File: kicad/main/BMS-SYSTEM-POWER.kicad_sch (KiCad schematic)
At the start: 67 parts, among them Q11 2N3904, Q15 IRLML6344TRPBF, Q16 IRLML6344TRPBF, Q17 AO4407A, Q2 AO4407A, Q3 PNP-SOT23, U21 AP64501SP-13, U22 AP64501SP-13, U5 SY8089A

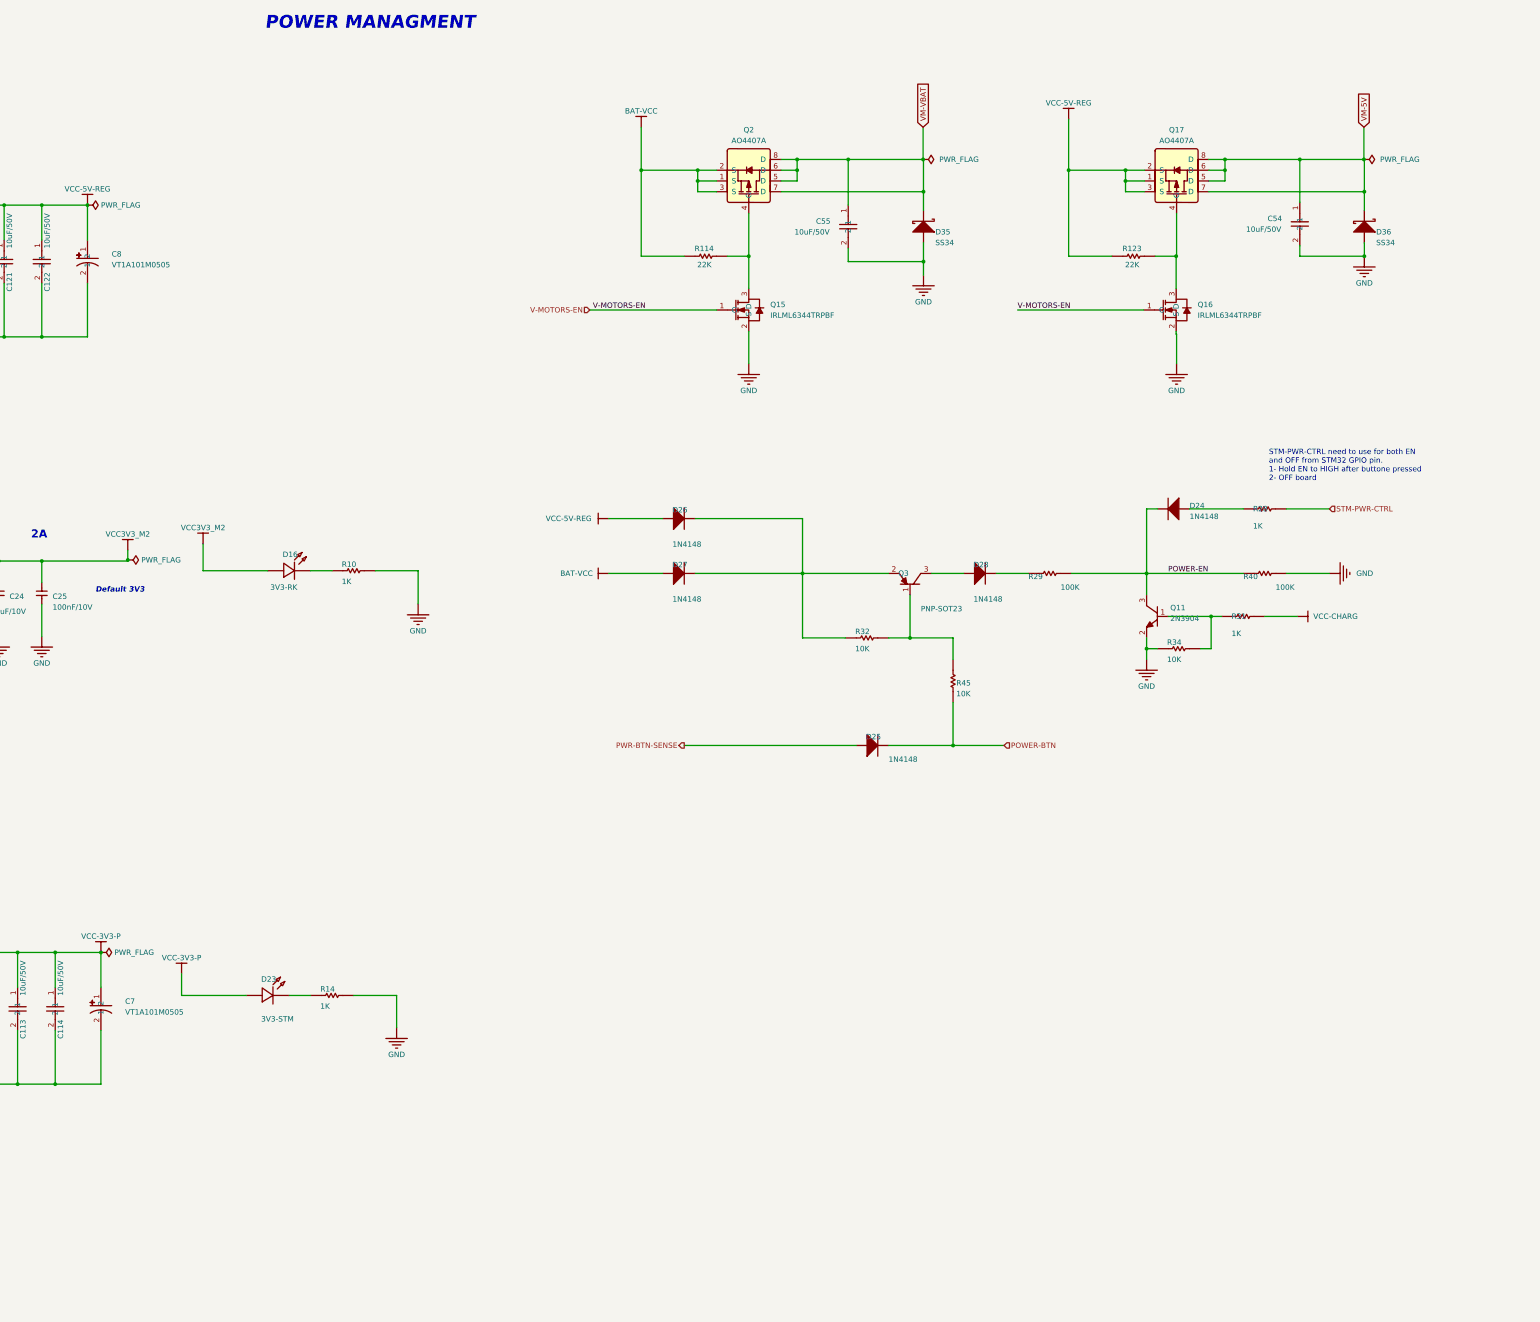
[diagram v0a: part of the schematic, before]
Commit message: Fix edge cut; no-CM STEP
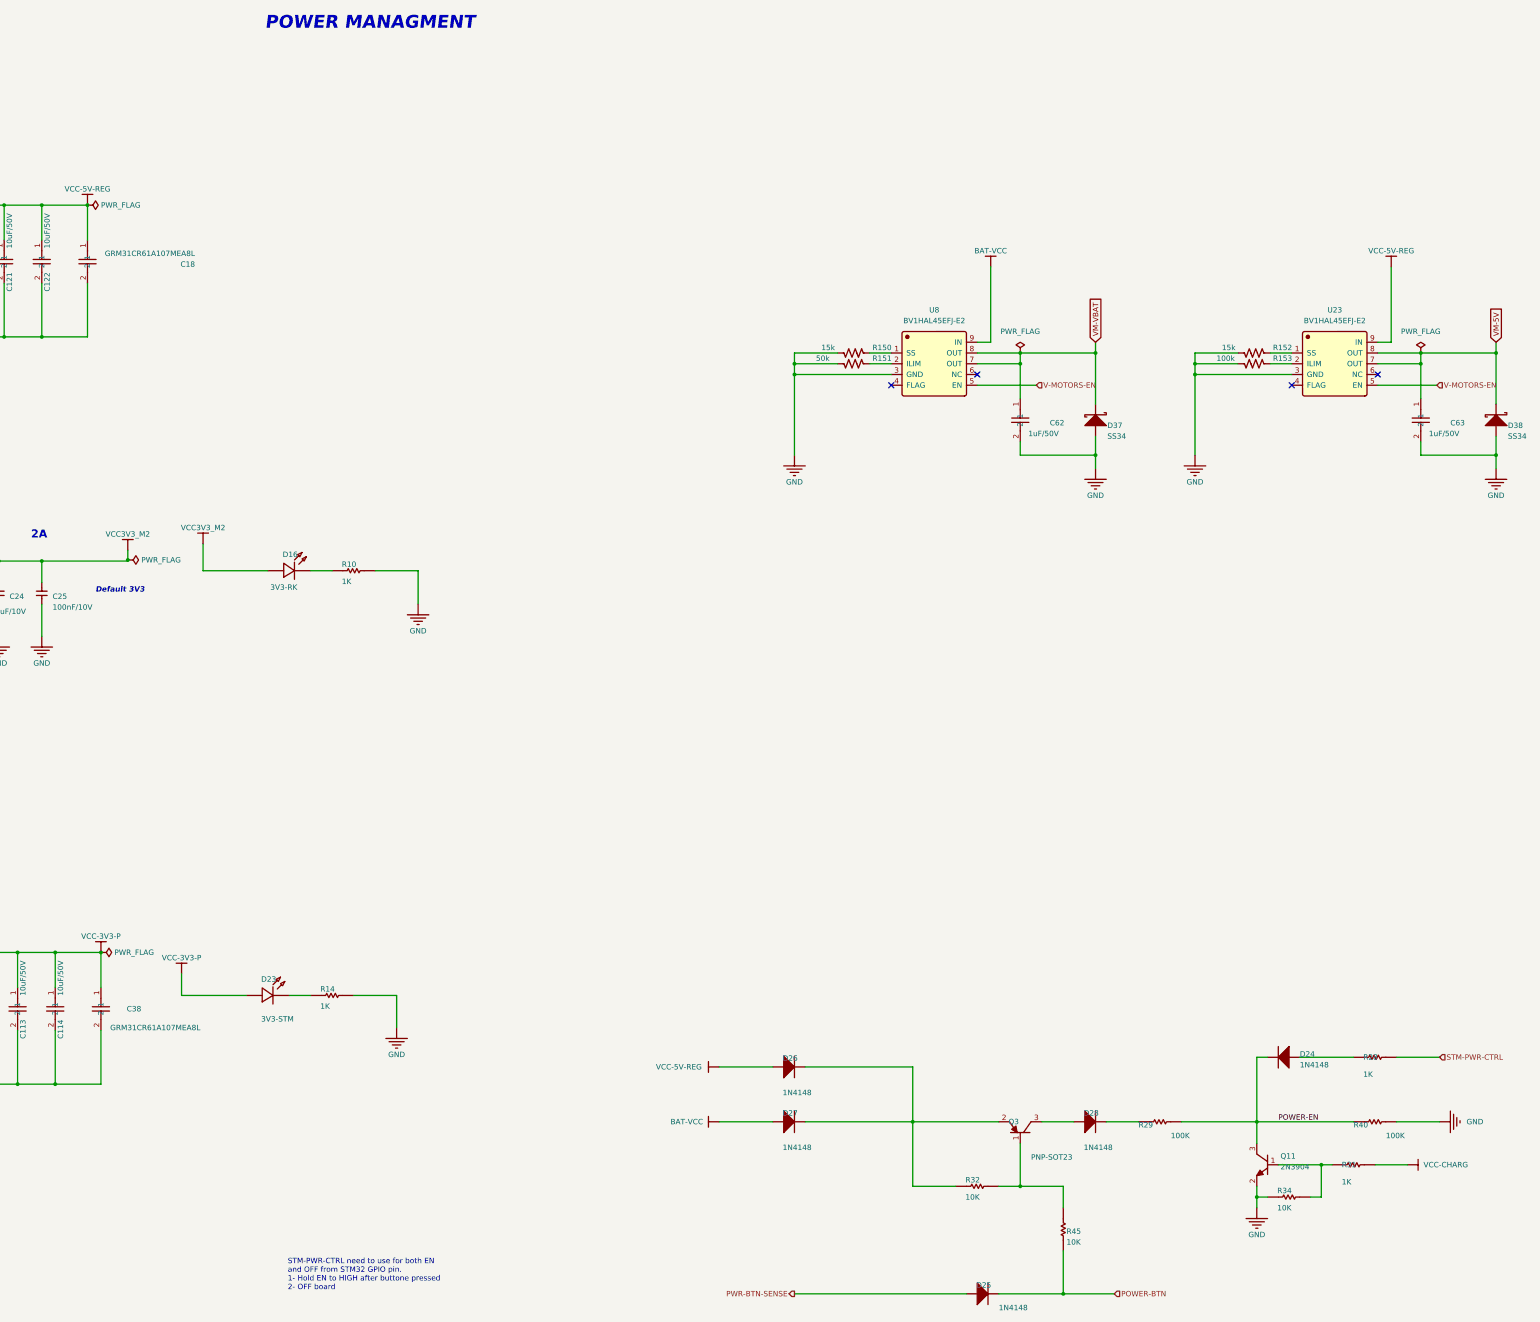
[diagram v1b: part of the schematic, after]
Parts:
- removed C54, C55: 10uF/50V, Capacitor_SMD:C_0603_1608Metric, symbol JLCImport:CL21A106KBYQNNE
- removed C7, C8: VT1A101M0505, JLCImport:VT1A101M0505, symbol JLCImport:VT1A101M0505
- removed D35, D36: SS34, oomwoo_altium:SMA, symbol DesignLibrary:MAIN-BRUSH MOTOR_1_DIODE-2_DesignLibrary.SchLib
- removed Q15, Q16: IRLML6344TRPBF, JLCImport:IRLML6344TRPBF, symbol JLCImport:IRLML6344TRPBF
- removed Q17, Q2: AO4407A, JLCImport:AO4407A, symbol JLCImport:AO4407A
- removed R114, R123: 22K, Resistor_SMD:R_0603_1608Metric, symbol DesignLibrary:MAIN-FAN_0_Resistor-1_DesignLibrary.SchLib
- added C18, C38: GRM31CR61A107MEA8L, JLCImport:GRM31CR61A107MEA8L, symbol JLCImport:GRM31CR61A107MEA8L
- added C62, C63: 1uF/50V, Capacitor_SMD:C_0603_1608Metric, symbol JLCImport:CL21A106KBYQNNE
- added D37, D38: SS34, oomwoo_altium:SMA, symbol DesignLibrary:MAIN-BRUSH MOTOR_1_DIODE-2_DesignLibrary.SchLib
- added R150, R152: 15k, Resistor_SMD:R_0603_1608Metric, symbol Device:R_US
- added R151: 50k, Resistor_SMD:R_0603_1608Metric, symbol Device:R_US
- added R153: 100k, Resistor_SMD:R_0603_1608Metric, symbol Device:R_US
- added U23, U8: BV1HAL45EFJ-E2, JLCImport:BV1HAL45EFJ-E2, symbol JLCImport:BV1HAL45EFJ-E2
- R141, R143, R144, R145, R146, R147, R148, R149: footprint (none) -> Resistor_SMD:R_0603_1608Metric
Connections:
- net BAT-VCC: now also U8.9 (IN)
- net GND: now also C18.2, C38.2, C62.2, C63.2, D37.1 (A), D38.1 (A), R150.1, R151.1, R152.1, R153.1, U23.3 (GND), U8.3 (GND)
- net V-MOTORS-EN: now also U23.5 (EN), U8.5 (EN)
- net VCC-3V3-P: now also C38.1
- net VCC-5V-REG: now also C18.1, U23.9 (IN)
- net VM-5V: now also C63.1, D38.2 (K), U23.7 (OUT), U23.8 (OUT)
- net VM-VBAT: now also C62.1, D37.2 (K), U8.7 (OUT), U8.8 (OUT)
- new net: R153.2, U23.2 (ILIM)
- new net: R152.2, U23.1 (SS)
- new net: R150.2, U8.1 (SS)
- new net: R151.2, U8.2 (ILIM)
- no-connect marks 0 -> 4
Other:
- moved on the sheet: D24, D25, D26, D27, D28, Q11, Q3, R28, R29, R31, R32, R34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

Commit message: Schematic fixes, 1st round of review
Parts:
- removed C18, C38: GRM31CR61A107MEA8L, JLCImport:GRM31CR61A107MEA8L, symbol JLCImport:GRM31CR61A107MEA8L
- removed C24, C27: 22uF/10V, Capacitor_SMD:C_0603_1608Metric, symbol DesignLibrary:POWER_1_Capacitor-1_DesignLibrary.SchLib
- removed C25: 100nF/10V, Capacitor_SMD:C_0603_1608Metric, symbol DesignLibrary:POWER_1_Capacitor-1_DesignLibrary.SchLib
- removed C26: 20pF/10V, Capacitor_SMD:C_0603_1608Metric, symbol DesignLibrary:POWER_2_Capacitor-1_DesignLibrary.SchLib
- removed D16: 3V3-RK, oomwoo_altium:LED0603-B, symbol DesignLibrary:POWER_0_LED-SMD_DesignLibrary.SchLib
- removed L5: 2.2uH, oomwoo_altium:IND-SMD_L4.4-W4.2, symbol DesignLibrary:POWER_0_INDUCTOR-SMD_DesignLibrary.SchLib
- removed Q3: PNP-SOT23, oomwoo_altium:SOT23-3D, symbol DesignLibrary:POWER_1_mirrored_PNP-SOT23_DesignLibrary.SchLib
- removed R10: 1K, Resistor_SMD:R_0603_1608Metric, symbol DesignLibrary:POWER_2_Resistor-1_DesignLibrary.SchLib
- removed R23: 100K, Resistor_SMD:R_0603_1608Metric, symbol DesignLibrary:POWER_0_Resistor-1_DesignLibrary.SchLib
- removed R24: 450K, Resistor_SMD:R_0603_1608Metric, symbol DesignLibrary:POWER_2_Resistor-1_DesignLibrary.SchLib
- removed R26: 100K, Resistor_SMD:R_0603_1608Metric, symbol DesignLibrary:POWER_3_Resistor-1_DesignLibrary.SchLib
- removed U5: SY8089A, oomwoo_altium:SOT5P95B160_300H130, symbol DesignLibrary:POWER_0_SY8089A_0_DesignLibrary.SchLib
- added C104, C124, C131, C132, C140, C141, C144, C145, C146, C147: 10uF/25V, Capacitor_SMD:C_0603_1608Metric, symbol JLCImport:CL21A106KBYQNNE
- added C127, C128, C129: 100nF/50V, Capacitor_SMD:C_0603_1608Metric, symbol Library:C_0603
- added C130: 1.2nF/50V, Capacitor_SMD:C_0603_1608Metric, symbol Library:C_0603
- added L4: CYA0630-3_3UH, JLCImport:CYA0630-3_3UH, symbol JLCImport:CYA0630-3_3UH
- added Q12: 2N3906_C49023424, JLCImport:2N3906_C49023424, symbol JLCImport:2N3906_C49023424
- added R10, R16, R58, R59: 100k, Resistor_SMD:R_0603_1608Metric, symbol Device:R_US
- added R154: 10, Resistor_SMD:R_0603_1608Metric, symbol Device:R_US
- added R155: 12k, Resistor_SMD:R_0603_1608Metric, symbol Device:R_US
- added R156: 69.8k, Resistor_SMD:R_0603_1608Metric, symbol Device:R_US
- added R157: 22.1k, Resistor_SMD:R_0603_1608Metric, symbol Device:R_US
- added R158: 100, Resistor_SMD:R_0805_2012Metric, symbol Device:R_US
- added R23: 10k, Resistor_SMD:R_0603_1608Metric, symbol Device:R_US
- added U1: NCP1117ST33T3G, NCP1117ST33T3G:SOT230P700X180-4N, symbol NCP1117ST33T3G:NCP1117ST33T3G
- added U24: AP64501SP-13, JLCImport:AP64501SP-13, symbol JLCImport:AP64501SP-13
- C102, C107, C111, C117, C118, C119: LCSC C1590 -> C1591
- C106, C113, C114, C115, C116, C121, C122, C95: value 10uF/50V -> 10uF/25V; LCSC C2932476 -> C96446; MPN CL21A106KBYQNNE -> (none); Manufacturer Part CL21A106KBYQNNE -> (none)
- C62, C63: value 1uF/50V -> 10uF/25V; LCSC C2932476 -> C96446; MPN CL21A106KBYQNNE -> (none); Manufacturer Part CL21A106KBYQNNE -> (none)
- D23: LCSC (none) -> C19171394; MANUFACTURER * -> (none); Manufacturer (none) -> *
- D24, D25, D26, D27, D28: LCSC (none) -> C917030; MANUFACTURER * -> (none); Manufacturer (none) -> *
- D37, D38: footprint oomwoo_altium:SMA -> Diode_SMD:D_SMA; LCSC (none) -> C22448055; MANUFACTURER * -> (none); Manufacturer (none) -> *
- Q11: LCSC (none) -> C50176433; MANUFACTURER * -> (none); Manufacturer (none) -> *
- R14, R28: value 1K -> 1k; MANUFACTURER * -> (none); Manufacturer (none) -> *
- R150, R152: value 15k -> 10k
- R151: value 50k -> 47k
- R29, R40: value 100K -> 100k; MANUFACTURER * -> (none); Manufacturer (none) -> *
- R31: value 1K -> 10k; MANUFACTURER * -> (none); Manufacturer (none) -> *
- R32, R34, R45: value 10K -> 10k; MANUFACTURER * -> (none); Manufacturer (none) -> *
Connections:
- net BAT-VCC: now also C104.1, C124.1, C127.1, R158.2, U24.2 (VIN); no longer U21.3 (EN), U22.3 (EN)
- net GND: now also C104.2, C124.2, C127.2, C128.2, C130.2, C131.2, C132.2, C140.2, C141.2, C144.2, C145.2, C146.2, C147.2, R10.2, R157.1, R16.2, R58.2, R59.2, U1.1 (GND), U24.7 (GND), U24.9 (EP)
- net POWER-EN: now also U22.3 (EN)
- net V-MOTORS-EN: now also R58.1, R59.1
- net VCC-3V3-P: now also C146.1
- net VCC-5V-REG: now also C147.1
- net VCC3V3_M2: now also C131.1, C132.1, C144.1, C145.1, L4.2, R156.2
- net at D26.2 (K), D27.2 (K), R32.2: now also Q12.2 (E)
- net at R32.1, R45.2: now also Q12.1 (B)
- net at D28.1 (A): now also Q12.3 (C)
- new net: C130.1, R155.1
- new net: R155.2, U24.6 (COMP)
- new net: R156.1, R157.2, U24.5 (FB)
- new net: C140.1, R158.1, U1.3 (IN)
- new net: L4.1, R154.2, U24.8 (SW)
- new net: C129.2, U24.1 (BST)
- new net: C128.1, U24.4 (SS)
- new net: C129.1, R154.1
- new net +3.3VP: R16.1, R23.1, U21.3 (EN)
- new net 3.3VBAT: C141.1, U1.2 (OUT), U1.4 (OUT__1)
- new net M2_PWR_EN: R10.1, R23.2, U24.3 (EN)
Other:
- note removed: "2A"
- note removed: "Default 3.3V"
- note removed: "Default 3V3"
- moved on the sheet: C102, C106, C107, C111, C112, C113, C114, C62, C63, C95, D23, D37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
